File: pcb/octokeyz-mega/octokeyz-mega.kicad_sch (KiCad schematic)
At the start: 36 parts, among them J1 USB_B_Mini, J2 PIN H 5P, J3 PIN S 4P, SW1 Gateron KS-3, SW2 Gateron KS-3, SW3 Gateron KS-3, SW4 Gateron KS-3, SW5 Gateron KS-3, SW6 Gateron KS-3, SW7 Gateron KS-3, SW8 Gateron KS-3, U1 USBLC6-2SC6, U2 MCP1700-3302E, U3 STM32F042K6T6

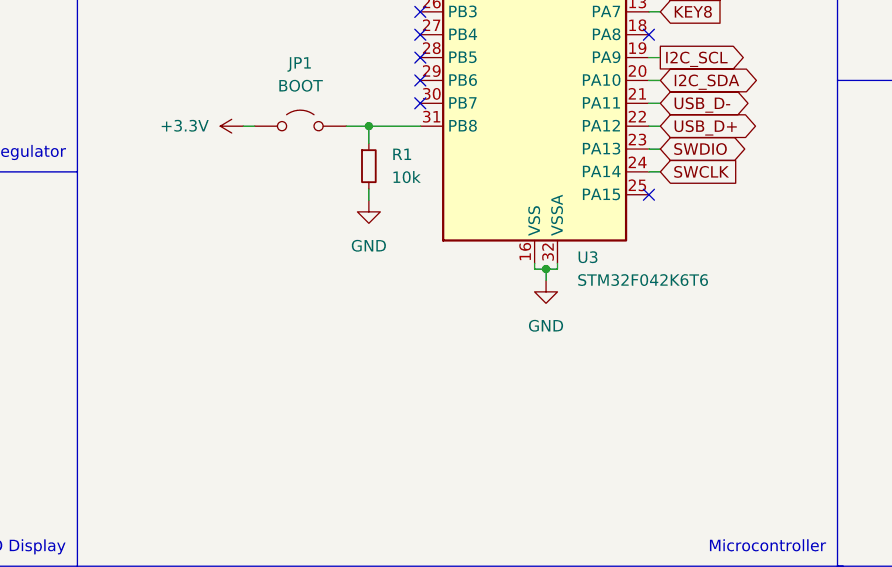
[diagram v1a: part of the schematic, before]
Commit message: pcb: added STM32F042K4T6 as microcontroller alternative
as this is a purely cosmetic change that doesn't affects the produced
boards I do not bumped revision number neither re-generated gerber
files.
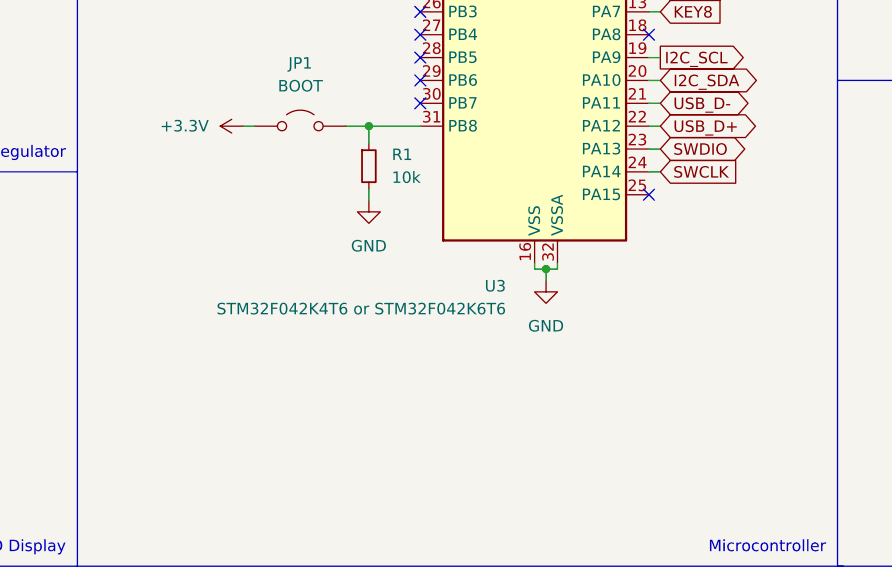
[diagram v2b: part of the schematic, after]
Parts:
- U3: value STM32F042K6T6 -> STM32F042K4T6 or STM32F042K6T6
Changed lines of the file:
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@@
 		(on_board yes)
 		(dnp no)
-		(fields_autoplaced yes)
 		(property "Reference" "U3"
-			(at 171.7391 118.11 0)
+			(at 163.83 121.285 0)
 			(effects
 				(font
 					(size 1.27 1.27)
 				)
-				(justify left)
+				(justify right)
 			)
 		)
-		(property "Value" "STM32F042K6T6"
-			(at 171.7391 120.65 0)
+		(property "Value" "STM32F042K4T6 or STM32F042K6T6"
+			(at 163.83 123.825 0)
 			(effects
 				(font
 					(size 1.27 1.27)
 				)
-				(justify left)
+				(justify right)
 			)
 		)

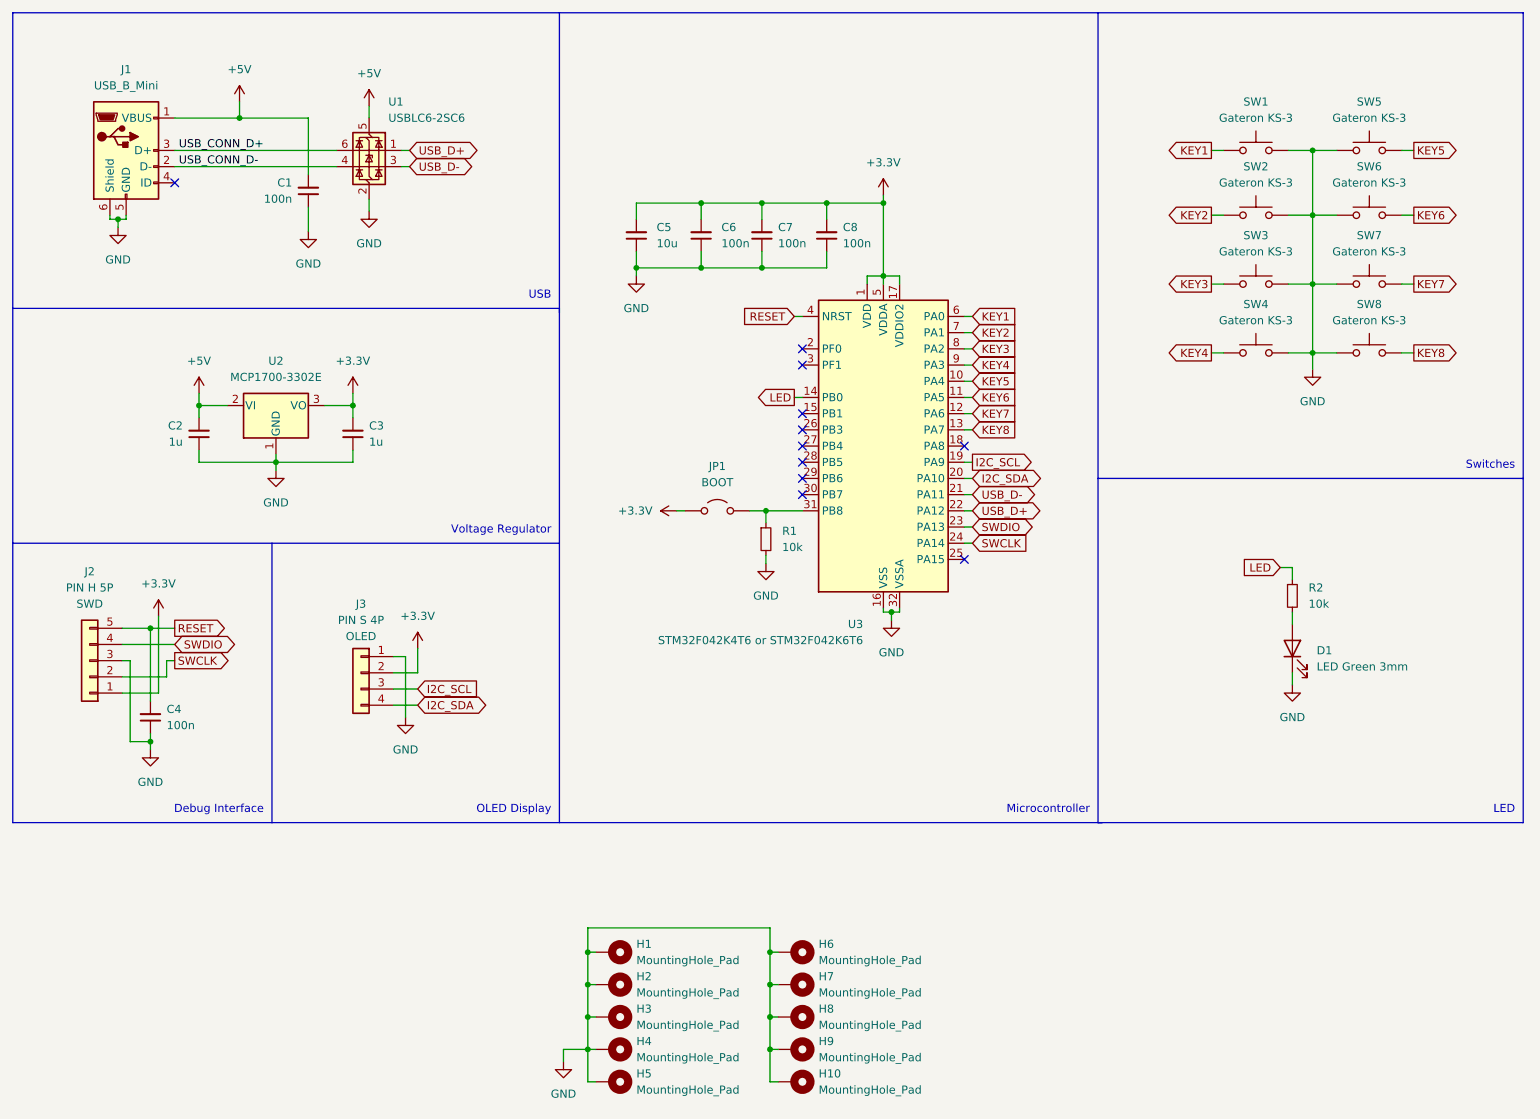
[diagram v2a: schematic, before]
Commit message: pcb: upgrade to kicad 9
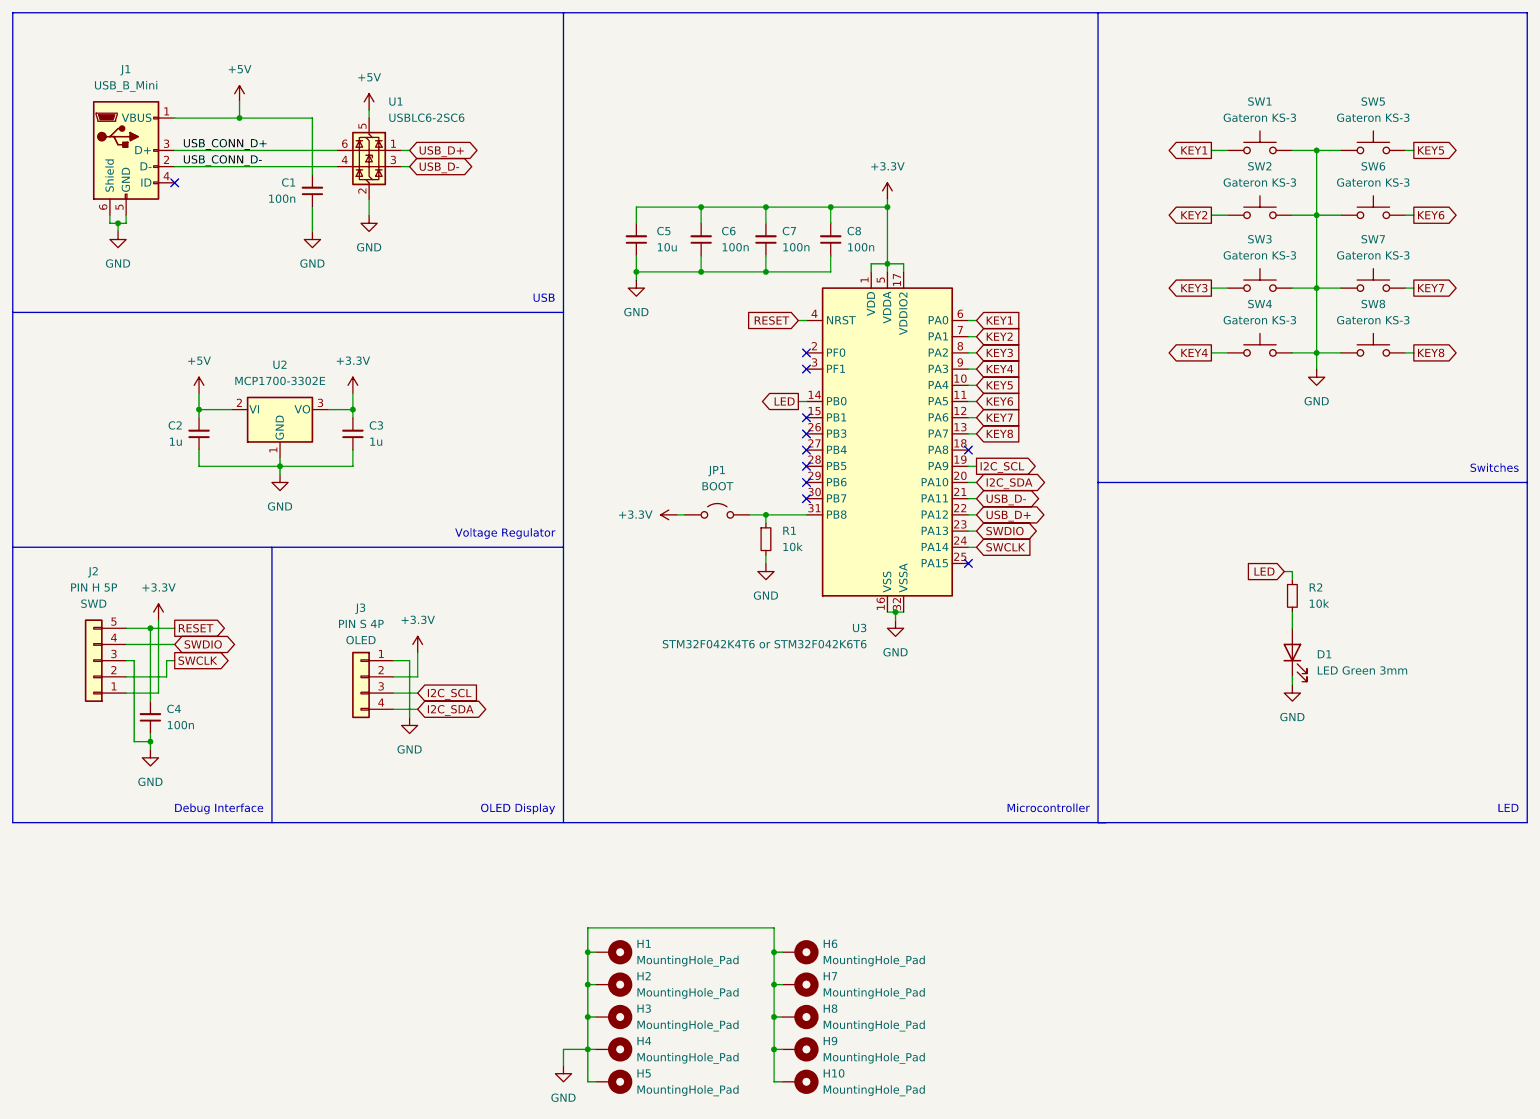
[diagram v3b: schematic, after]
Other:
- moved on the sheet: C1, C5, C6, C7, C8, D1, H10, H6, H7, H8, H9, J2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
